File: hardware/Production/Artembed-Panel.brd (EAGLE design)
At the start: 108.4 x 142.2 mm, 494 parts, among them J12 CORTEX_JTAG_DEBUG_MINIMUM_PTH, J13 CORTEX_JTAG_DEBUG_PTH_NS, J16 CAMERA-HIMAX, J21 CORTEX_JTAG_DEBUG_MINIMUM_PTH, J22 CORTEX_JTAG_DEBUG_PTH_NS, J25 CAMERA-HIMAX, J3 CORTEX_JTAG_DEBUG_MINIMUM_PTH, J30 CORTEX_JTAG_DEBUG_MINIMUM_PTH, J31 CORTEX_JTAG_DEBUG_PTH_NS, J34 CAMERA-HIMAX, J4 CORTEX_JTAG_DEBUG_PTH_NS, J7 CAMERA-HIMAX, U1 DAPLINK_KL26Z, U10 LIS2DH12, U11 DAPLINK_KL26Z, U12 16MHz, U13 ARTEMIS_MODULESMD, U14 1.8V, U15 LIS2DH12, U16 DAPLINK_KL26Z, U17 16MHz, U18 ARTEMIS_MODULESMD, U19 1.8V, U2 16MHz, U20 LIS2DH12, U3 ARTEMIS_MODULESMD, U4 1.8V, U5 LIS2DH12, U6 DAPLINK_KL26Z, U7 16MHz, U8 ARTEMIS_MODULESMD, U9 1.8V, Y1 32.768kHz, Y2 32.768kHz, Y3 32.768kHz, Y4 32.768kHz

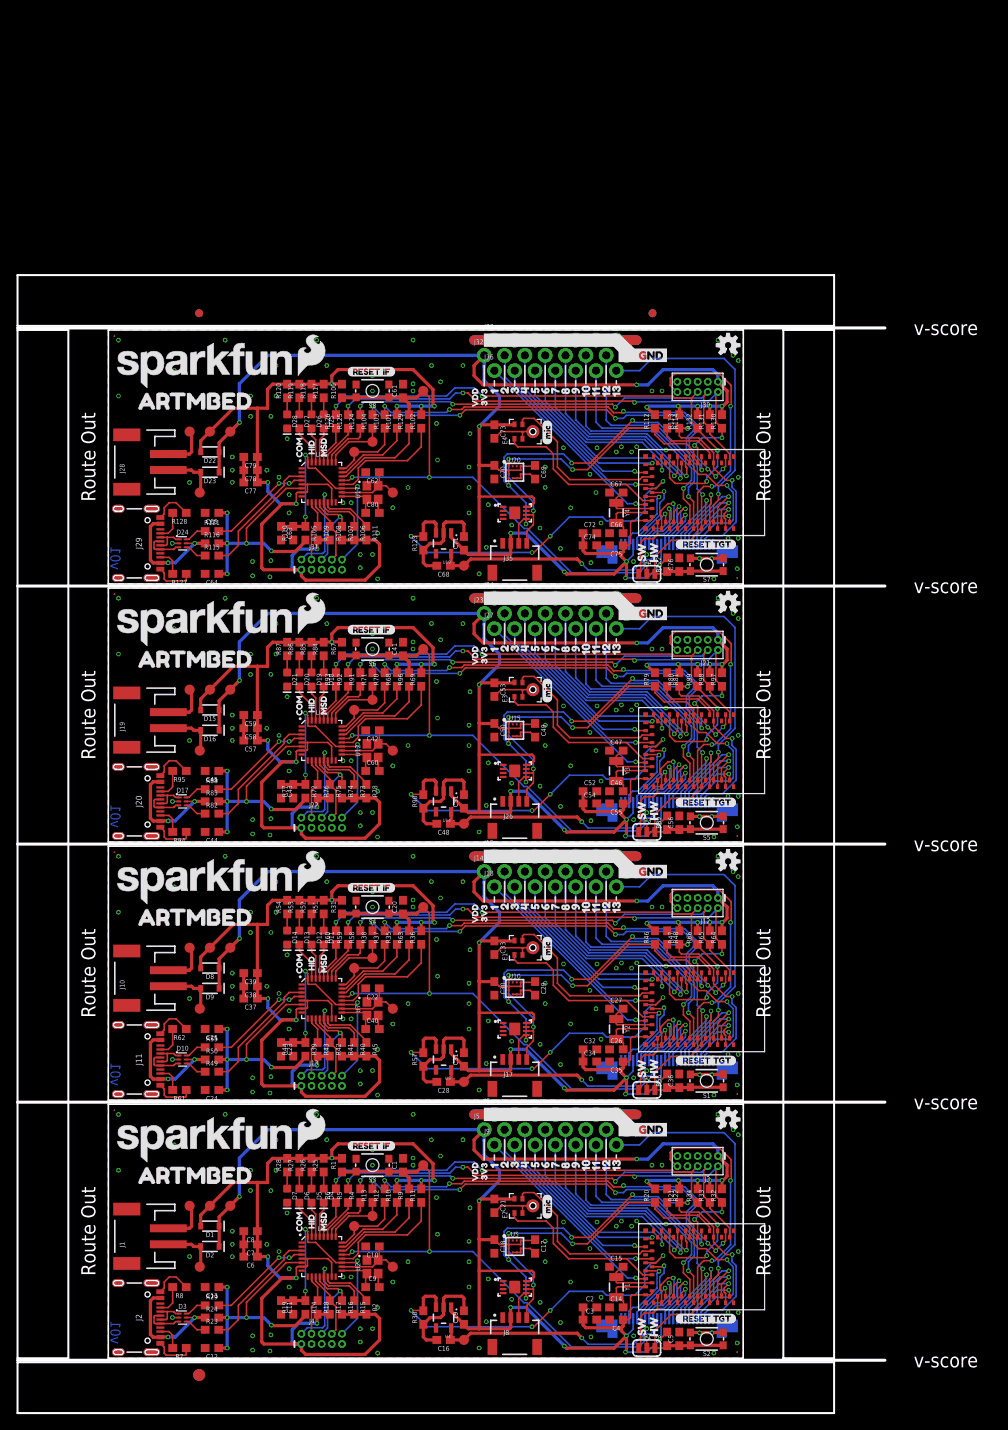
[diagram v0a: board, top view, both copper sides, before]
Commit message: panelized + cammed
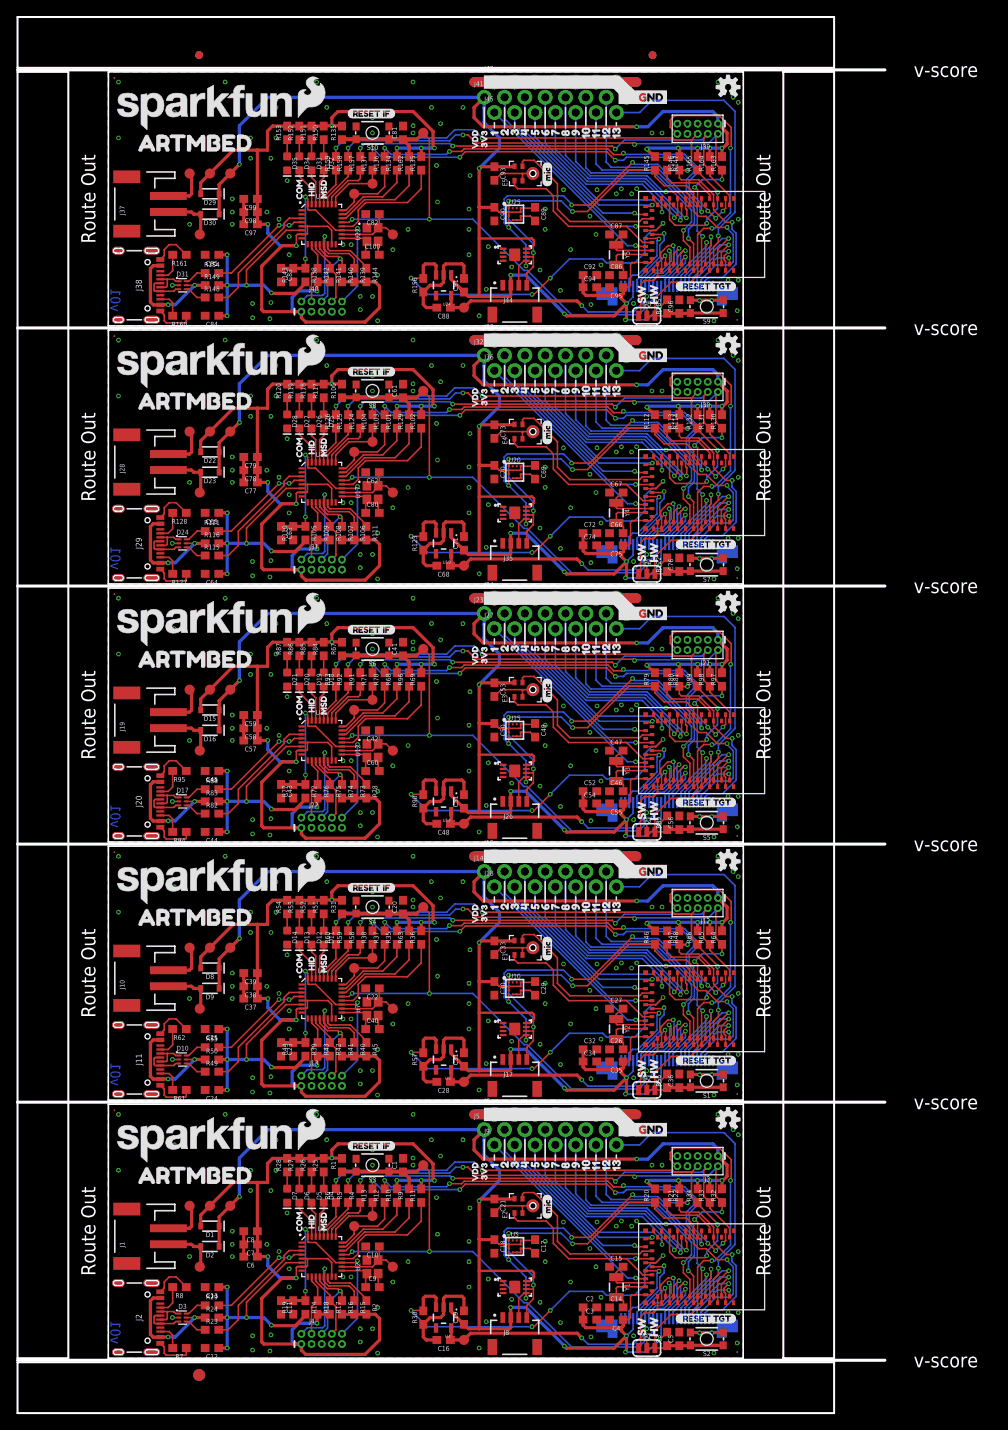
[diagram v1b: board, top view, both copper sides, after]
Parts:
- added C100, C82: 12pF, SparkFun-Capacitors:0603
- added C81, C83, C85, C89, C95, C98, C99: 0.1uF, SparkFun-Capacitors:0603
- added C84, C88, C91, C93, C94: 1.0uF, SparkFun-Capacitors:0603
- added C86, C87: 15pF, SparkFun-Capacitors:0603
- added C90, C92: 10uF, SparkFun-Capacitors:0603
- added C96: 1nF, SparkFun-Capacitors:0603
- added C97: 2.2uF, SparkFun-Capacitors:0603
- added D29, D30: 3A/10V/280mV, SparkFun-DiscreteSemi:SOD-323
- added D31: PRTR5V0U2F, SparkFun-IC-Power:SOT886
- added D32: BLUE, SparkFun-LED:LED-0603
- added D33: GREEN, SparkFun-LED:LED-0603
- added D34: Yellow, SparkFun-LED:LED-0603
- added D35: RED, SparkFun-LED:LED-0603
- added E5: SPH0641LM4H-1, SparkFun-Sensors:SPH0641LM4H-1_MICROPHONE
- added ECC5: ATECC508AUDFN_2X3MM, ATECC508A:UDFN_2X3MM
- added FD17, FD18, FD19, FD20: FIDUCIAL0.2MM, SparkFun-Aesthetics:FIDUCIAL-0.2MM
- added J37: (no value), SparkFun-Connectors:JST-2-SMD
- added J38: (no value), SparkFun-Connectors:USB-C-16P
- added J39: CORTEX_JTAG_DEBUG_MINIMUM_PTH, SparkFun-Connectors:2X5-PTH-1.27MM
- added J40: CORTEX_JTAG_DEBUG_PTH_NS, SparkFun-Connectors:2X5-PTH-1.27MM-NO_SILK
- added J41: (no value), SparkFun-Connectors:1X08_NO_SILK
- added J42, J45: (no value), SparkFun-Connectors:1X07_NO_SILK
- added J43: CAMERA-HIMAX, SparkFun-Connectors:FPC-24-AMPHENOL-SFV24R-1STE1HLF
- added J44: (no value), SparkFun-Connectors:JST04_1MM_RA
- added JP5: HW/SW RESET, SparkFun-Jumpers:SMT-JUMPER_3_1-NC_TRACE_SILK
- added LOGO10: SFE_LOGO_NAME.2_INCH, SparkFun-Aesthetics:SFE_LOGO_NAME_.2
- added LOGO9: OSHW-LOGOS, SparkFun-Aesthetics:OSHW-LOGO-S
- added R133, R143, R144, R147, R155, R156: 10k, SparkFun-Resistors:0603
- added R134, R135, R139, R140, R141, R142, R163, R164, R165: DNP, SparkFun-Resistors:0603
- added R136, R137, R157, R158, R159, R162: 0, SparkFun-Resistors:0603
- added R138: 5.62k, SparkFun-Resistors:0603
- added R145, R146: 2.2k, SparkFun-Resistors:0603
- added R148, R154: 33, SparkFun-Resistors:0603
- added R149: 10, SparkFun-Resistors:0603
- added R150, R151, R152, R153: 330, SparkFun-Resistors:0603
- added R160, R161: 5.1k, SparkFun-Resistors:0603
- added S10: RESET IF, SparkFun-Switches:TACTILE_SWITCH_SMD_4.6X2.8MM
- added S9: RESET TGT, SparkFun-Switches:TACTILE_SWITCH_SMD_4.6X2.8MM
- added TP37: TEST-POINT3X5, SparkFun-Connectors:PAD.03X.05
- added TP38, TP39, TP40, TP41, TP42, TP43, TP44, TP45: (no value), SparkFun-Connectors:PAD.03X.05
- added U$109: (no value), temp_buzzard_labels:10
- added U$110: (no value), temp_buzzard_labels:21
- added U$111: (no value), temp_buzzard_labels:32
- added U$112: (no value), temp_buzzard_labels:43
- added U$113: (no value), temp_buzzard_labels:54
- added U$114: (no value), temp_buzzard_labels:65
- added U$115: (no value), temp_buzzard_labels:76
- added U$116: (no value), temp_buzzard_labels:87
- added U$117: (no value), temp_buzzard_labels:98
- added U$118: (no value), temp_buzzard_labels:109
- added U$119: (no value), temp_buzzard_labels:1110
- added U$120: (no value), temp_buzzard_labels:1211
- added U$121: (no value), temp_buzzard_labels:1312
- added U$122: (no value), temp_buzzard_labels:GND13
- added U$123: (no value), SparkFun-Aesthetics:SFE_LOGO_FLAME_.2
- added U$124: (no value), temp_buzzard_labels:ARTMBED17
- added U$125: (no value), SparkFun-Aesthetics:QWIIC_4MM
- added U$126: (no value), buzzard_labels_1:COM7
- added U$127: (no value), buzzard_labels_1:HID5
- added U$128: (no value), buzzard_labels_1:MSD6
- added U$129: (no value), buzzard_labels_1:MIC0
- added U$130: (no value), buzzard_labels_1:HW3
- added U$131: (no value), buzzard_labels_1:SW4
- added U$132: (no value), buzzard_labels_1:_RESET_TGT2
- added U$133: (no value), buzzard_labels_1:RESET_IF1
- added U$134: (no value), buzzard_labels_1:3V39
- added U$135: (no value), buzzard_labels_1:VDD8
- added U21: DAPLINK_KL26Z, artembed:QFN-32-NOPAD
- added U22: 16MHz, SparkFun-Clocks:CRYSTAL-SMD-2X2.5MM
- added U23: ARTEMIS_MODULESMD, SparkFun-IC-Microcontroller:ARTEMIS_FP
- added U24: 1.8V, SparkFun-IC-Power:SOT23-5
- added U25: LIS2DH12, SparkFun-Sensors:LGA-12-LISDH12
- added Y5: 32.768kHz, SparkFun-Clocks:CRYSTAL-SMD-3.2X1.5MM
- moved E$1 32.3 mm to (11.3, 162.9)
- moved E$2 32.3 mm to (11.3, 162.9)
- moved E$3 32.3 mm to (68.0, 162.9)
- moved E$4 32.3 mm to (68.0, 162.9)
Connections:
- new net !RST4: C83.1, J40.10, R138.1, R143.2, U21.19, U21.32
- new net !TGT_RST!_HW4: C96.1, J39.10, JP5.3, R155.1, S9.3, S9.4, U23.~RST
- new net !TGT_RST!_SW4: JP5.1, U23.~D19
- new net !TGT_RST4: C81.1, JP5.2, R133.1, R162.2, S10.3, S10.4, TP39.P$1, U21.21
- new net 1.8V4: C88.1, J43.10, TP37.P$1, U24.5
- new net 3.3V4: C97.1, C98.1, C99.1, D29.A, J40.1, R133.2, R134.2, R135.2, R139.2, R140.2, R141.2, R142.2, R144.2, R150.2, R151.2, R152.2, R153.2, TP41.P$1, U21.15, U21.5, U21.7
- new net CAMERA_D32: J43.3, U23.AD34
- new net CAMERA_D33: J43.5, U23.~AD33/SWO
- new net CAMERA_D34: J43.12, U23.D41
- new net CAMERA_D35: J43.20, U23.~D44
- new net CAMERA_D36: J43.19, U23.~D37
- new net CAMERA_D37: J43.13, U23.~D45
- new net CAMERA_D38: J43.14, U23.~D43
- new net CAMERA_D39: J43.9, U23.~AD31
- new net CAMERA_DVDD_EN4: R156.2, U23.D15, U24.3
- new net CAMERA_HSYNC4: J43.16, U23.~D42
- new net CAMERA_INT4: J43.18, U23.D38
- new net CAMERA_MCLK4: J43.8, U23.~D18
- new net CAMERA_PCLK4: J43.17, U23.D36
- new net CAMERA_TRIG4: J43.7, U23.D17
- new net CAMERA_VSYNC4: J43.6, U23.AD16
- new net D53: J45.7, U23.D3
- new net D54: J45.1, U23.~AD29
- new net D55: J41.2, U23.~AD13
- new net D56: J45.2, U23.~D25
- new net D57: J41.3, U23.~D6
- new net D58: J45.3, U23.~D27
- new net D59: J41.4, U23.~D4
- new net D60: J45.4, U23.~AD35
- new net D61: J41.5, U23.D7
- new net D62: J45.5, U23.~D5
- new net D63: J41.6, U23.D2
- new net D64: J45.6, U23.D1
- new net D65: J41.7, U23.D0
- new net GND4: C100.2, C81.2, C82.2, C83.2, C84.2, C85.2, C86.1, C87.1, C88.2, C89.2, C90.2, C91.2, C92.2, C93.2, C94.2, C95.2, C96.2, C97.2, C98.2, C99.2, D31.2, D35.C, E5.2, E5.3, E5.6, E5.7, E5.8, ECC5.4, ECC5.P, J37.2, J38.GND, J38.GND2, J39.3, J39.5, J39.9, J40.3, J40.5, J40.9, J41.8, J42.1, J42.2, J42.3, J42.4, J42.5, J42.6, J42.7, J43.15, J43.2, J44.1, R143.1, R147.1, R156.1, R160.1, R161.1, S10.1, S10.2, S9.1, S9.2, TP45.P$1, U21.16, U21.2, U21.8, U22.P2, U22.P4, U23.GND@1, U23.GND@22, U23.GND@38, U23.GND@39, U23.GND@47, U23.GND@59, U24.2, U25.5, U25.6, U25.7, U25.8
- new net LED_HID4: D33.C, U21.30
- new net LED_MSD4: D32.C, U21.29
- new net LED_UART4: D34.C, U21.31
- new net N$100: D35.A, R153.1
- new net N$101: R144.1, U21.14
- new net N$102: C100.1, U21.17, U22.P1
- new net N$103: C82.1, TP44.P$1, U21.18, U22.P3
- new net N$104: R135.1, U21.20
- new net N$105: R134.1, U21.23
- new net N$106: D30.A, J37.1, TP40.P$1
- new net N$107: R162.1, U21.22
- new net N$108: R157.1, U21.26
- new net N$109: R158.1, U21.27
- new net N$110: R159.1, U21.28
- new net N$111: C86.2, U23.XI, Y5.P$2
- new net N$112: C87.2, U23.XO, Y5.P$1
- new net N$113: R136.1, TP42.P$1, U21.24
- new net N$114: R137.1, TP43.P$1, U21.25
- new net N$115: R147.2, U23.BOOT
- new net N$93: D32.A, R150.1
- new net N$94: D33.A, R151.1
- new net N$95: D34.A, R152.1
- new net N$96: J38.B5, R160.2
- new net N$97: J38.A5, R161.2
- new net N$98: D31.4, R148.1
- new net N$99: D31.6, R154.1
- new net PDM_CLK4: E5.4, U23.~AD12
- new net PDM_DATA4: E5.1, U23.~AD11
- new net SCL4: ECC5.6, J43.21, J44.4, R145.1, U23.D8, U25.1
- new net SDA4: ECC5.5, J43.22, J44.3, R146.1, U23.D9, U25.4
- new net TCLK4: J40.4, R142.1, U21.10
- new net TDI4: J40.8, R141.1, U21.11
- new net TDO4: J40.6, R140.1, U21.12
- new net TGT_RX4: R137.2, U23.TXO-0
- new net TGT_SWCLK4: J39.4, R157.2, R164.1, U23.SWDCK
- new net TGT_SWDIO4: J39.2, R158.2, R163.1, U23.SWDIO
- new net TGT_SWO4: J39.6, R159.2, R165.1, U23.~D22
- new net TGT_TX4: R136.2, U23.RXI-0
- new net TMS4: J40.2, R139.1, U21.13
- new net USB_D+_P4: R148.2, U21.3
- new net USB_D+_R4: D31.3, J38.A6, J38.B6
- new net USB_D-_P4: R154.2, U21.4
- new net USB_D-_R4: D31.1, J38.A7, J38.B7
- new net VBUS_IF8: D31.5, J38.VBUS1, J38.VBUS2, R149.1
- new net VBUS_IF9: C84.1, C85.1, R138.2, R149.2, U21.6
- new net VDD4: C89.1, C90.1, C91.1, C92.1, C93.1, C94.1, C95.1, D29.C, D30.C, E5.5, ECC5.8, J39.1, J41.1, J43.11, J43.4, J44.2, R145.2, R146.2, R155.2, R163.2, R164.2, R165.2, TP38.P$1, U23.VDD@36, U23.VDD@37, U24.1, U25.10, U25.2, U25.3, U25.9
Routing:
- net VDD4: track 0.00 -> 206.0 mm, vias 0 -> 13
- net 3.3V4: track 0.00 -> 116.6 mm, vias 0 -> 7
- net GND4: track 0.00 -> 82.7 mm, vias 0 -> 84
- net !TGT_RST4: track 0.00 -> 68.9 mm, vias 0 -> 3
- net TGT_SWO4: track 0.00 -> 68.1 mm, vias 0 -> 4
- net SDA4: track 0.00 -> 63.8 mm, vias 0 -> 6
- net TGT_SWDIO4: track 0.00 -> 61.4 mm, vias 0 -> 5
- net SCL4: track 0.00 -> 59.1 mm, vias 0 -> 4
- net TGT_SWCLK4: track 0.00 -> 56.2 mm, vias 0 -> 3
- net TGT_TX4: track 0.00 -> 53.0 mm, vias 0 -> 6
- net TGT_RX4: track 0.00 -> 51.5 mm, vias 0 -> 4
- net !TGT_RST!_HW4: track 0.00 -> 49.0 mm, vias 0 -> 2
- net CAMERA_DVDD_EN4: track 0.00 -> 46.1 mm, vias 0 -> 4
- net D53: track 0.00 -> 36.2 mm, vias 0 -> 1
- net VBUS_IF9: track 0.00 -> 32.5 mm, vias 0 -> 5
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- added copper zone on layer 1, net GND4
- added copper zone on layer 16, net GND4
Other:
- board size 108.4 x 142.2 mm -> 108.4 x 174.5 mm
